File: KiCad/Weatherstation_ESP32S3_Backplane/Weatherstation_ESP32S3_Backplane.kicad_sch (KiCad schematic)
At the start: 48 parts, among them J1 01x02 JST XH, J10 01x04 Molex KK254, J11 01x02 JST XH, J12 01x04 Molex KK254, J13 01x22 Generic socket, J14 01x22 Generic socket, J15 01x02 JST XH, J16 01x04 Molex KK254, J17 01x02 JST XH, J18 01x06 Generic socket, J19 01x06 Generic socket, J2 01x03 JST XH, J3 01x03 JST XH, J4 01x07 Generic socket, J5 01x08 Generic socket, J6 01x08 Generic socket, J7 01x04 JST XH, J8 01x04 Molex KK254, J9 282834-2 Screw Terminal, Q1 RFP12N10L, U1 LM7805, U2 MAX6675ISA+T

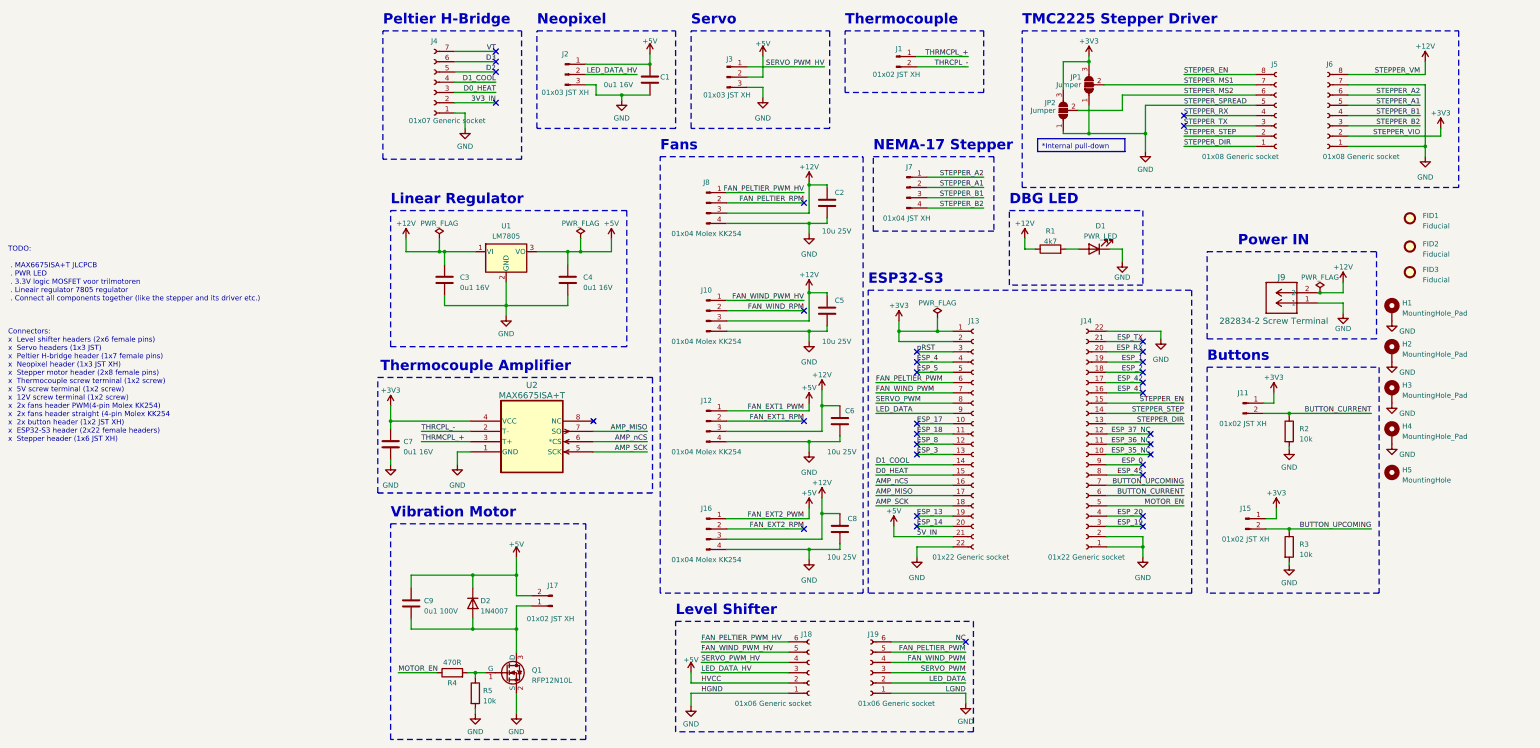
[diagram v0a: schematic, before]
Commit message: Added DBG_LED, flat-mount LM7805, GPIO breakout header
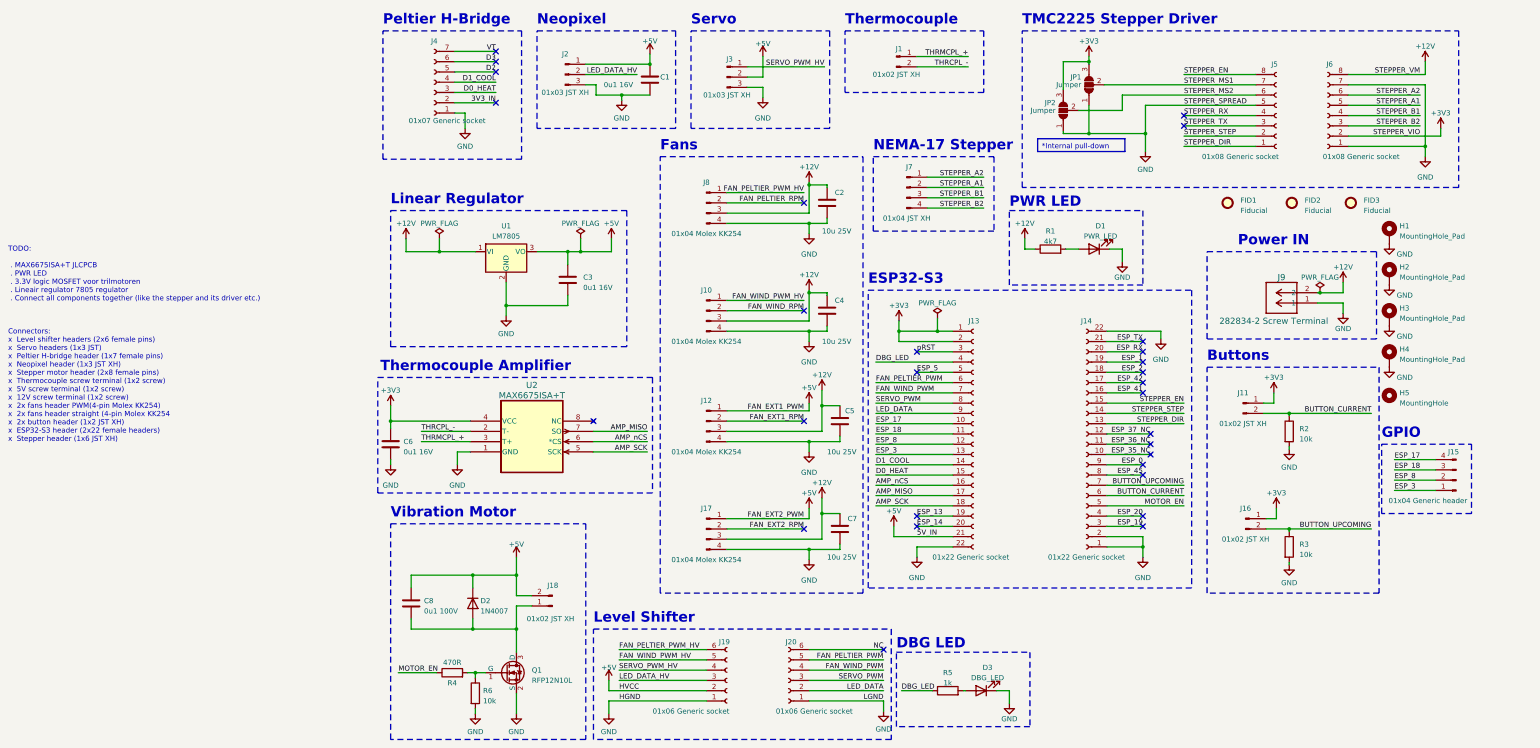
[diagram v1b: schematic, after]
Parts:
- removed C3: 0u1 16V, Capacitor_SMD:C_0402_1005Metric, symbol Device:C
- added D3: DBG_LED, LED_SMD:LED_0805_2012Metric, symbol Device:LED
- added J15: 01x04 Generic header, Connector_PinHeader_2.54mm:PinHeader_1x04_P2.54mm_Vertical, symbol Connector:Conn_01x04_Pin
- added R5: 1k, Resistor_SMD:R_0805_2012Metric, symbol Device:R
- U1: footprint Package_TO_SOT_THT:TO-220-3_Vertical -> Package_TO_SOT_THT:TO-220-3_Horizontal_TabDown
- renumbered C4 to C3, C5 to C4, C6 to C5, C7 to C6, C8 to C7, C9 to C8, J15 to J16, J16 to J17, J17 to J18, J18 to J19, J19 to J20, R5 to R6
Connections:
- net ESP_17: now also J15.4 (Pin_4)
- net ESP_18: now also J15.3 (Pin_3)
- net ESP_3: now also J15.1 (Pin_1)
- net ESP_8: now also J15.2 (Pin_2)
- net GND: now also D3.1 (K)
- net ESP_4 renamed DBG_LED
- net DBG_LED: now also R5.1
- new net: D3.2 (A), R5.2
- no-connect marks 34 -> 29
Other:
- note added: "GPIO"
- note added: "PWR LED"
- moved on the sheet: FID1, FID2, FID3, H1, H2, H3, H4, H5, J19, J20

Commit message: Added QoL and stability features
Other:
- note added: "Tactiel weerstation Backplane"
- note removed: "TODO: . MAX6675ISA+T JLCPCB . PWR LED . 3.3V logic MOSFET voor trilmotoren . Lineair regulator 7805 regulator . Connect all components together (like the stepper and its driver etc.) Connectors: x Level shifter headers (2x6 female pins) x Servo headers (1x3 JST) x Peltier H-bridge header (1x7 female pins) x Neopixel header (1x3 JST XH) x Stepper motor header (2x8 female pins) x Thermocouple screw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"
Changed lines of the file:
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@@
     (at 177.165 45.72 0) (size 21.59 3.175)
     (stroke (width 0) (type default))
-    (fill (type color) (color 255 255 194 1))
+    (fill (type none))
     (effects (font (size 1.27 1.27)) (justify left top))
   )
@@
   (text "Linear Regulator" (at 17.145 62.23 0)
     (effects (font (size 2.54 2.54) (thickness 0.508) bold) (justify left bottom))
+  )
+  (text "Tactiel weerstation Backplane" (at 185.42 176.53 0)
+    (effects (font (size 4 4) (thickness 0.8) bold) (justify left bottom))
   )
   (text "Peltier H-Bridge" (at 15.24 17.78 0)
@@
     (effects (font (size 2.54 2.54) (thickness 0.508) bold) (justify left bottom))
   )
-  (text "TODO:\n\n . MAX6675ISA+T JLCPCB\n . PWR LED\n . 3.3V logic MOSFET voor trilmotoren\n . Lineair regulator 7805 regulator\n . Connect all components together (like the stepper and its driver etc.)\n\n\n\nConnectors:\nx  Level shifter headers (2x6 female pins)\nx  Servo headers (1x3 JST)\nx  Peltier H-bridge header (1x7 female pins)\nx  Neopixel header (1x3 JST XH)\nx  Stepper motor header (2x8 female pins)\nx  Thermocouple screw terminal (1x2 screw)\nx  5V screw terminal (1x2 screw)\nx  12V screw terminal (1x2 screw)\nx  2x fans header PWM(4-pin Molex KK254)\nx  2x fans header straight (4-pin Molex KK254\nx  2x button header (1x2 JST XH)\nx  ESP32-S3 header (2x22 female headers)\nx  Stepper header (1x6 JST XH)\n\n\n\n"
-    (at -77.47 127 0)
-    (effects (font (size 1.27 1.27)) (justify left bottom))
-  )
   (text "Power IN" (at 226.695 72.39 0)
